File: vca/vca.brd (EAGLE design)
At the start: 43.2 x 224.8 mm, 59 parts, among them IC1 OPA4130U, IC2 OPA134D, Q1 BC847ALT1SMD, X1 2516-

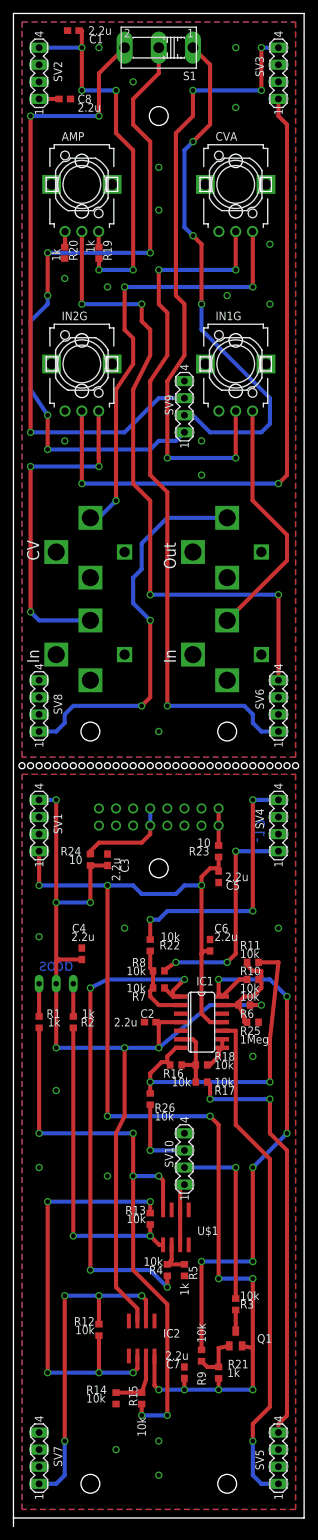
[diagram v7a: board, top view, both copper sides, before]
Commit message: almost finished vcf2 and vca 2nd rev.  Need to verify mechanical dimensions
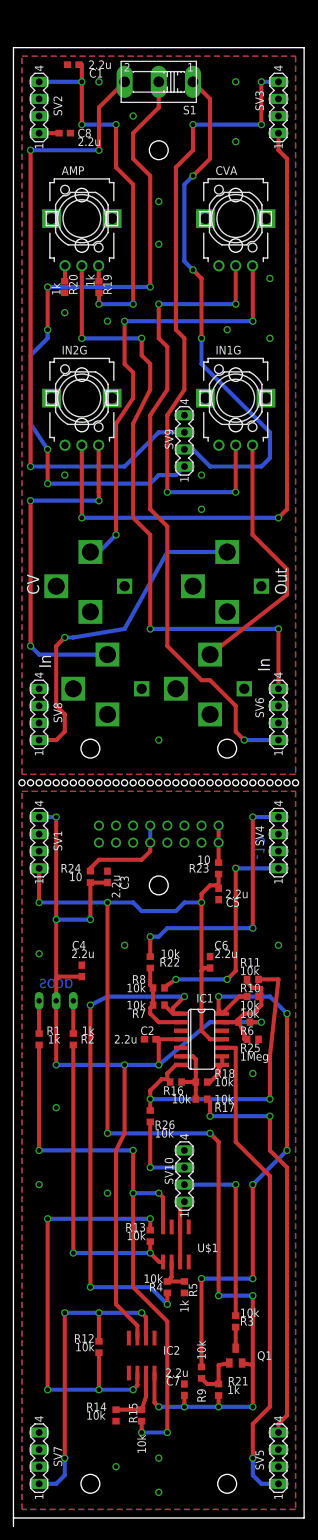
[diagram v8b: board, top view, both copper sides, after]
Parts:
- moved IN2 5.68 mm to (14.0, 123.2)
- moved IN1 5.68 mm to (29.2, 123.2)
- moved AMP 5.08 mm to (10.2, 193.0)
- moved CVA 5.08 mm to (33.0, 193.0)
- moved R19 5.08 mm to (12.7, 182.9)
- moved R20 5.08 mm to (7.62, 182.9)
- moved C1 5.08 mm to (8.89, 215.9)
- moved C8 5.08 mm to (7.62, 205.7)
- moved CVIN 5.08 mm to (11.4, 138.4)
- moved IN1G 5.08 mm to (33.0, 166.4)
- moved IN2G 5.08 mm to (10.2, 166.4)
- moved OUT 5.08 mm to (31.8, 138.4)
- moved S1 5.08 mm to (21.6, 213.4)
- moved SV2 5.08 mm to (3.81, 209.6)
- moved SV3 5.08 mm to (39.4, 209.6)
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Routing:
- net N$31: track 103.1 -> 94.8 mm
- net N$5: track 58.1 -> 50.3 mm, vias 2 -> 1
- net N$32: track 96.8 -> 93.0 mm
- net N$27: track 49.4 -> 51.9 mm
- net N$18: track 50.7 -> 48.1 mm
- net N$24: track 62.7 -> 60.2 mm
- net N$33: track 75.5 -> 73.0 mm
- net N$25: track 36.9 -> 38.8 mm
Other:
- board size 43.2 x 224.8 mm -> 43.2 x 219.7 mm
